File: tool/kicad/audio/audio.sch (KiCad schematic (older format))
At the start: 146 parts, among them J1 MICRO-USB-AB, K1 CONN_3, K2 CONN_3, P1 TEST_POINT, P10 TEST_POINT, P11 TEST_POINT, P12 TEST_POINT, P13 TEST_POINT, P14 TEST_POINT, P15 TEST_POINT, P16 TEST_POINT, P17 TEST_POINT, P18 TEST_POINT, P19 TEST_POINT, P2 TEST_POINT, P20 TEST_POINT, P21 TEST_POINT, P22 TEST_POINT, P23 TEST_POINT, P24 TEST_POINT, P25 TEST_POINT, P26 TEST_POINT, P27 TEST_POINT, P28 TEST_POINT, P29 TEST_POINT, P3 TEST_POINT, P30 CONN_3X2, P31 CONN_2, P32 CONN_2, P33 TEST_POINT, P34 TEST_POINT, P35 CONN_6, P37 TEST_POINT, P38 TEST_POINT, P4 TEST_POINT, P5 MIDI-IN, P6 TEST_POINT, P7 TEST_POINT, P8 TEST_POINT, P9 TEST_POINT, U1 SN74LVC2T45, U2 ST-USBLC6-2, U3 EFM32GG332, U4 YM2413, U5 LM386, U6 LM386, U7 ACPL-M21L, X1 48Mhz, X2 CRYSTAL

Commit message: fix and layout audio/midi board
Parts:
- removed C1, C11: 10uF, symbol C
- removed C10, C8: 10nF, symbol C
- removed C12, C24: 4.7uF, symbol C
- removed C15, C16: 20pF/NC, symbol C
- removed C17, C2, C3, C5: 100nF, symbol C
- removed C4, C6: 18pF, symbol C
- removed C7, C9: 1uF, symbol C
- removed D1, D10, D11, D2, D3, D4, D5, D6, D7, D8, D9: LED, symbol LED
- removed J1: MICRO-USB-AB, symbol MICRO-USB-AB
- removed JP1, JP2, JP3, JP4, JP5: SJ, symbol SJ
- removed K1: CONN_3, symbol CONN_3
- removed L1, L2, L3: FB, symbol L
- removed L4: L, symbol L
- removed P1, P10, P11, P12, P13, P14, P15, P16, P17, P18, P19, P2, P20, P21, P22, P23, P24, P25, P26, P27, P28, P29, P3, P33, P34, P37, P38, P4, P6, P7, P8, P9: TEST_POINT, symbol TEST_POINT
- removed P30: CONN_3X2, symbol CONN_3X2
- removed P31, P32: CONN_2, symbol CONN_2
- removed P35: CONN_6, symbol CONN_6
- removed R1, R10, R13, R2, R3, R4, R5, R6, R7, R8, R9: 3k3, symbol R
- removed R11: 1, symbol R
- removed R12, R14: 15, symbol R
- removed R17, R18, R19, R20, R21, R22, R23, R24, R25, R26, R27, R28, R32, R34: 22, symbol R
- removed R31, R35: 100k, symbol R
- removed R36: 100k/NC, symbol R
- removed R38, R42: 100, symbol R
- removed R45, R46, R47, R50: 2k2, symbol R
- removed S1, S2: TACTSW, symbol TACTSW
- removed U1: SN74LVC2T45, symbol SN74LVC2T45
- removed U2: ST-USBLC6-2, symbol ST-USBLC6-2
- removed U3: EFM32GG332, symbol EFM32GG332
- removed U4: YM2413, symbol YM2413
- removed X1: 48Mhz, symbol TXC-XTAL
- removed X2: CRYSTAL, symbol CRYSTAL
- added P1: CONN_6, symbol CONN_6
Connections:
- net labels removed: +3.3VADC, A0, A0', D+, D+B, D+_IN, D-, D-B, D-_IN, D0, D0', D1, D1', D2, D2', D3, D3', D4, D4', D5, D5', D6, D6', D7, D7', DEBUG_RX, DEBUG_TX, DECOUPLE, GI_2, G_I1, LED0, LED1, LED2, LED3, LED4, LED5, LED6, LED7, LED8, LED9, MOd2, ROd2, RXI, SWC, SWCU, SWD, SWO, TXO, USB_DMPU, VBUS_IN, XIN, XIN', XIN3V3, XOUT, XOUT', XOUT3V3, XTN, XTP, ~CS, ~CS', ~IC, ~IC', ~RESET, ~RESETD, ~WE, ~WE'
- wire segments 355 -> 89
- no-connect marks 17 -> 3
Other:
- moved on the sheet: C13, C14, C18, C19, C20, C21, C22, C23, D12, K2, P5, R15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

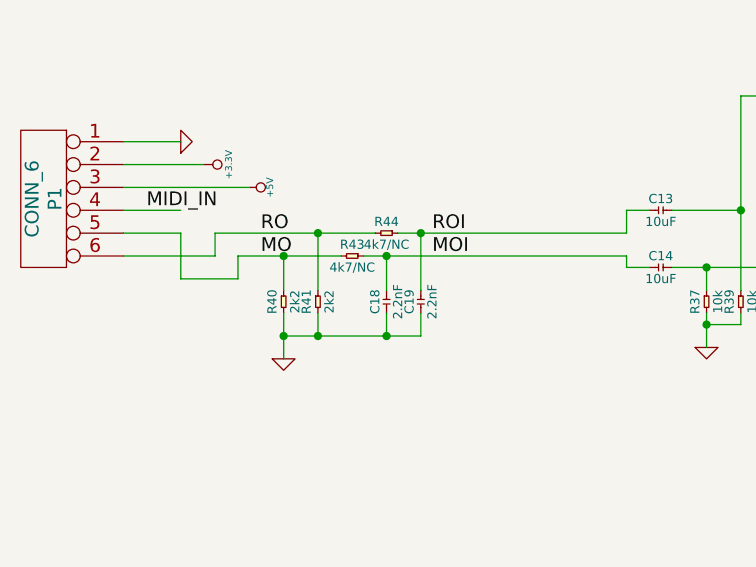
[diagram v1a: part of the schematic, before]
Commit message: adapt audio to don't have the 2k2s on this board by default
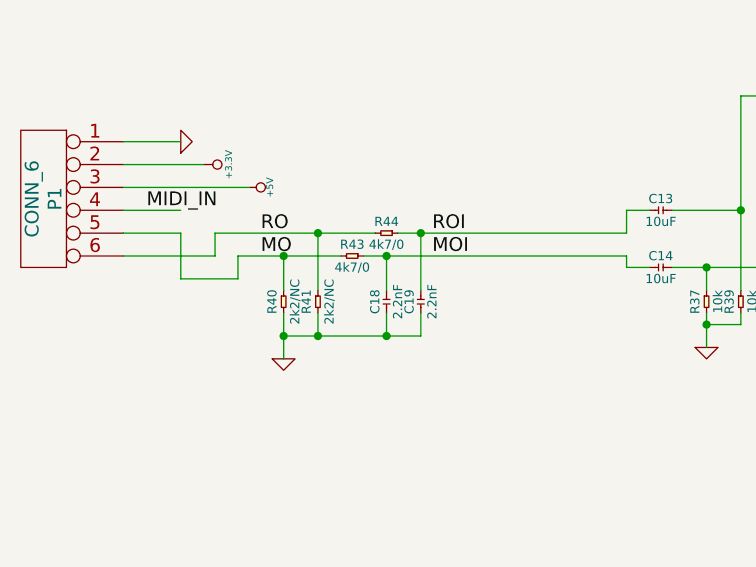
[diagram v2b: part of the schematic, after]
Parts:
- R40, R41: value 2k2 -> 2k2/NC
- R43, R44: value 4k7/NC -> 4k7/0
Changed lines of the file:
@@
 LIBS:contrib
 LIBS:valves
+LIBS:audio-cache
 EELAYER 24 0
 EELAYER END
@@
 P 2600 2300
 F 0 "R40" H 2600 2350 40  0000 C CNN
-F 1 "2k2" H 2600 2250 40  0000 C CNN
+F 1 "2k2/NC" H 2600 2250 40  0000 C CNN
 F 2 "" H 2600 2300 60  0000 C CNN
 F 3 "" H 2600 2300 60  0000 C CNN
@@
 P 2750 2300
 F 0 "R41" H 2750 2350 40  0000 C CNN
-F 1 "2k2" H 2750 2250 40  0000 C CNN
+F 1 "2k2/NC" H 2750 2250 40  0000 C CNN
 F 2 "" H 2750 2300 60  0000 C CNN
 F 3 "" H 2750 2300 60  0000 C CNN
@@
 P 3050 2000
 F 0 "R44" H 3050 2050 40  0000 C CNN
-F 1 "4k7/NC" H 3050 1950 40  0000 C CNN
+F 1 "4k7/0" H 3050 1950 40  0000 C CNN
 F 2 "" H 3050 2000 60  0000 C CNN
 F 3 "" H 3050 2000 60  0000 C CNN
@@
 P 2900 2100
 F 0 "R43" H 2900 2150 40  0000 C CNN
-F 1 "4k7/NC" H 2900 2050 40  0000 C CNN
+F 1 "4k7/0" H 2900 2050 40  0000 C CNN
 F 2 "" H 2900 2100 60  0000 C CNN
 F 3 "" H 2900 2100 60  0000 C CNN

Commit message: layout
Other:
- moved on the sheet: D12, P5, R15, U7
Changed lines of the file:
@@
 L CONN_5 P5
 U 1 1 52F74BDD
-P 5500 4500
-F 0 "P5" V 5450 4500 50  0000 C CNN
-F 1 "MIDI-IN" V 5550 4500 50  0000 C CNN
-F 2 "" H 5500 4500 60  0000 C CNN
-F 3 "" H 5500 4500 60  0000 C CNN
-	1    5500 4500
+P 2950 3200
+F 0 "P5" V 2900 3200 50  0000 C CNN
+F 1 "MIDI-IN" V 3000 3200 50  0000 C CNN
+F 2 "" H 2950 3200 60  0000 C CNN
+F 3 "" H 2950 3200 60  0000 C CNN
+	1    2950 3200
 	-1   0    0    1
 $EndComp
@@
 L R R15
 U 1 1 52F74BF4
-P 6050 4400
-F 0 "R15" H 6050 4450 40  0000 C CNN
-F 1 "220" H 6050 4350 40  0000 C CNN
-F 2 "" H 6050 4400 60  0000 C CNN
-F 3 "" H 6050 4400 60  0000 C CNN
-	1    6050 4400
+P 3500 3100
+F 0 "R15" H 3500 3150 40  0000 C CNN
+F 1 "220" H 3500 3050 40  0000 C CNN
+F 2 "" H 3500 3100 60  0000 C CNN
+F 3 "" H 3500 3100 60  0000 C CNN
+	1    3500 3100
 	-1   0    0    1
 $EndComp
@@
 Connection ~ 4450 2150
 Wire Wire Line
-	6100 4400 6200 4400
-Wire Wire Line
-	5900 4400 6000 4400
-Wire Wire Line
-	5950 4600 6250 4600
-Wire Wire Line
-	5950 4600 5950 4300
-Wire Wire Line
-	5950 4300 5900 4300
-Text Label 7000 4450 0    60   ~ 0
+	3550 3100 3650 3100
+Wire Wire Line
+	3350 3100 3450 3100
+Wire Wire Line
+	3400 3300 3700 3300
+Wire Wire Line
+	3400 3300 3400 3000
+Wire Wire Line
+	3400 3000 3350 3000
+Text Label 4450 3150 0    60   ~ 0
 MIDI_IN
 $Comp
 L D D12
 U 1 1 52F758D1
-P 6150 4500
-F 0 "D12" V 6100 4600 60  0000 C CNN
-F 1 "D" H 6155 4435 60  0001 C CNN
-F 2 "" H 6150 4500 60  0000 C CNN
-F 3 "" H 6150 4500 60  0000 C CNN
-	1    6150 4500
+P 3600 3200
+F 0 "D12" V 3550 3300 60  0000 C CNN
+F 1 "D" H 3605 3135 60  0001 C CNN
+F 2 "" H 3600 3200 60  0000 C CNN
+F 3 "" H 3600 3200 60  0000 C CNN
+	1    3600 3200
 	0    -1   -1   0
 $EndComp
 Wire Wire Line
-	6150 4400 6150 4450
-Connection ~ 6150 4400
-Wire Wire Line
-	6150 4550 6150 4600
-Connection ~ 6150 4600
+	3600 3100 3600 3150
+Connection ~ 3600 3100
+Wire Wire Line
+	3600 3250 3600 3300
+Connection ~ 3600 3300
 $Comp
 L CONN_3 K2
@@
 L ACPL-M21L U7
 U 1 1 52F8C674
-P 6650 4500
-F 0 "U7" H 6450 4900 60  0000 C CNN
-F 1 "ACPL-M21L" H 6300 4250 60  0001 C CNN
-F 2 "" H 6650 4500 60  0000 C CNN
-F 3 "" H 6650 4500 60  0000 C CNN
-	1    6650 4500
-	1    0    0    -1
-$EndComp
-Wire Wire Line
-	6250 4300 6200 4300
-Wire Wire Line
-	6200 4300 6200 4400
+P 4100 3200
+F 0 "U7" H 3900 3600 60  0000 C CNN
+F 1 "ACPL-M21L" H 3750 2950 60  0001 C CNN
+F 2 "" H 4100 3200 60  0000 C CNN
+F 3 "" H 4100 3200 60  0000 C CNN
+	1    4100 3200
+	1    0    0    -1
+$EndComp
+Wire Wire Line
+	3700 3000 3650 3000
+Wire Wire Line
+	3650 3000 3650 3100
 $Comp
 L GND #PWR010
 U 1 1 52F8C9F7
-P 6650 4850
-F 0 "#PWR010" H 6650 4850 30  0001 C CNN
-F 1 "GND" H 6650 4780 30  0001 C CNN
-F 2 "" H 6650 4850 60  0000 C CNN
-F 3 "" H 6650 4850 60  0000 C CNN
-	1    6650 4850
-	1    0    0    -1
-$EndComp
-Wire Wire Line
-	6650 4800 6650 4850
+P 4100 3550
+F 0 "#PWR010" H 4100 3550 30  0001 C CNN
+F 1 "GND" H 4100 3480 30  0001 C CNN
+F 2 "" H 4100 3550 60  0000 C CNN
+F 3 "" H 4100 3550 60  0000 C CNN
+	1    4100 3550
+	1    0    0    -1
+$EndComp
+Wire Wire Line
+	4100 3500 4100 3550
 $Comp
 L +3.3V #PWR011
 U 1 1 52F8CBAF
-P 6650 4050
-F 0 "#PWR011" H 6650 4010 30  0001 C CNN
-F 1 "+3.3V" H 6650 4160 30  0000 C CNN
-F 2 "" H 6650 4050 60  0000 C CNN
-F 3 "" H 6650 4050 60  0000 C CNN
-	1    6650 4050
-	1    0    0    -1
-$EndComp
-Wire Wire Line
-	6650 4050 6650 4100
-Wire Wire Line
-	7050 4450 6800 4450
-NoConn ~ 5900 4500
-NoConn ~ 5900 4600
-NoConn ~ 5900 4700
+P 4100 2750
+F 0 "#PWR011" H 4100 2710 30  0001 C CNN
+F 1 "+3.3V" H 4100 2860 30  0000 C CNN
+F 2 "" H 4100 2750 60  0000 C CNN
+F 3 "" H 4100 2750 60  0000 C CNN
+	1    4100 2750
+	1    0    0    -1
+$EndComp
+Wire Wire Line
+	4100 2750 4100 2800
+Wire Wire Line
+	4500 3150 4250 3150
+NoConn ~ 3350 3200
+NoConn ~ 3350 3300
+NoConn ~ 3350 3400
 Wire Wire Line
 	4100 2000 4100 1900
